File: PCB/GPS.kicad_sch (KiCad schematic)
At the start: 20 parts, among them CN2 Solder_Jumper-2_Open, U3 BGA725L6E6327FTSA1, U4 ST1S12GR, U5 B39162B4327P810, U6 TESEO-LIV3R

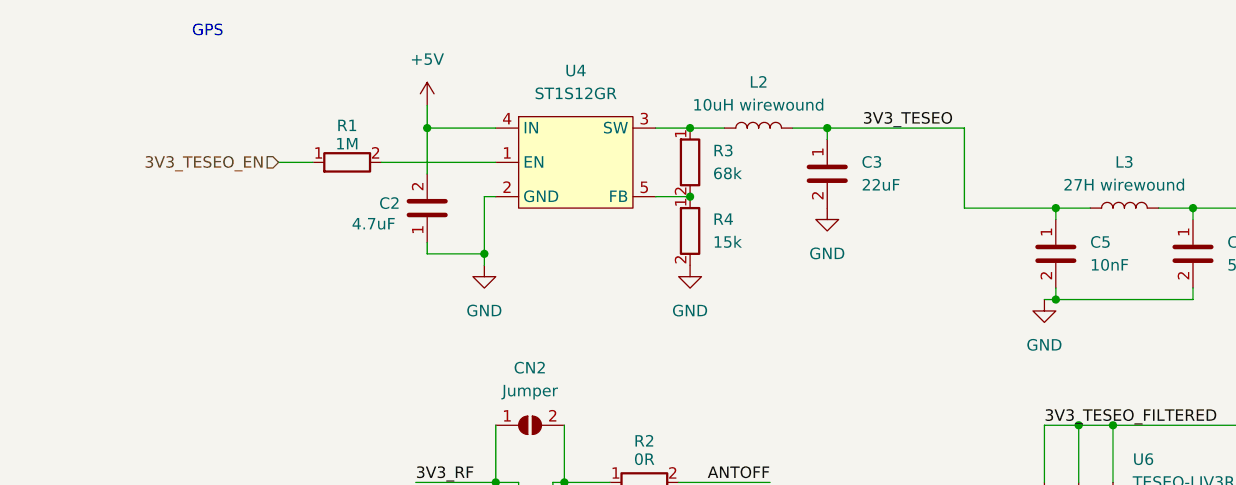
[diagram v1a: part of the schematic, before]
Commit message: Add LEDs
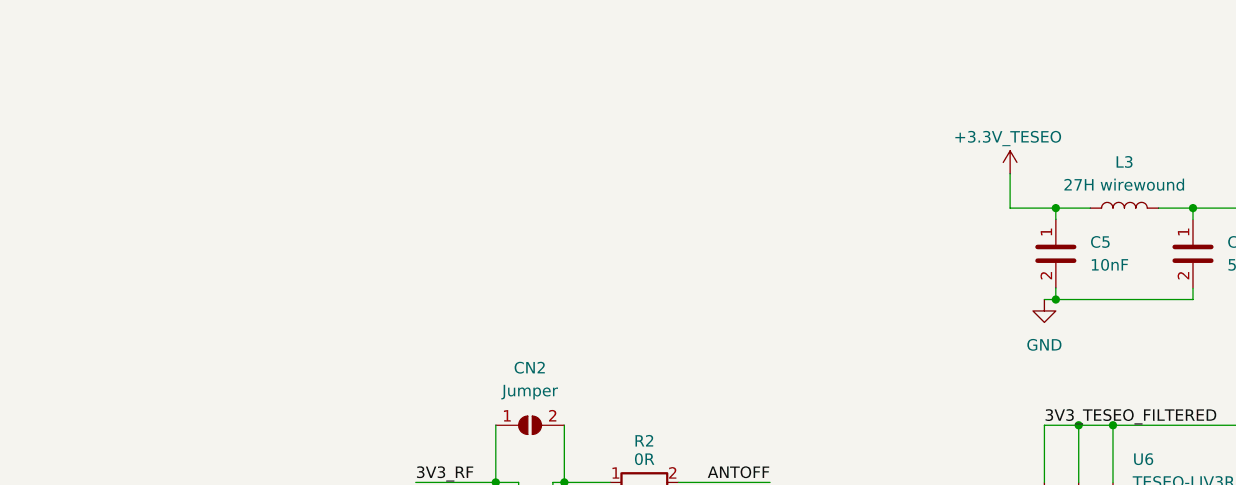
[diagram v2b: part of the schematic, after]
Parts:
- removed C2: C_4.7uF_10V_10%_X7S_0603_H0.95, 002-Capacitors:C_0603_H0.95, symbol 002-Capacitors:C_4.7uF_10V_10%_X7S_0603
- removed C3: C_22uF_6.3V_20%_X5R_0805_H1.4, 002-Capacitors:C_0805_H1.4, symbol 002-Capacitors:C_22uF_6.3V_20%_X5R_0805
- removed L2: L_10uH_20%_1.51A_160mOhm, 003-Inductors:LTF5022T-100M1R3-D, symbol 003-Inductors:L_10uH_20%_1.51A_160mOhm
- removed R1: R_1M_5%_1/16W_0402, 001-Resistors:R_0402_H0.4, symbol 001-Resistors:R_1M_5%_1/16W_0402
- removed R3: R_68k_1%_1/16W_0402, 001-Resistors:R_0402_H0.4, symbol 001-Resistors:R_68k_1%_1/16W_0402
- removed R4: R_15k_1%_1/16W_0402, 001-Resistors:R_0402_H0.4, symbol 001-Resistors:R_15k_1%_1/16W_0402
- removed U4: ST1S12GR, 004-Power:ST1S12GR, symbol 004-Power:ST1S12GR
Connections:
- net 3V3_TESEO renamed +3.3V_TESEO
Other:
- note removed: "GPS"

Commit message: Finish schematic minus mcu
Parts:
- added TP6, TP7, TP8: TP_square_1mm, 011-Misc:Testpoint_square_1mm, symbol 011-Misc:Testpoint_square_1mm
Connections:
- net TESEO_NRST: now also TP8.
- net TESEO_RX: now also TP7.
- net TESEO_TX: now also TP6.
- net +3.3V_TESEO renamed +3.3V
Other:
- note added: "GPS with passive antenna and LNA"

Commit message: Layout start
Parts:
- removed TP6, TP7, TP8: TP_square_1mm, 011-Misc:Testpoint_square_1mm, symbol 011-Misc:Testpoint_square_1mm
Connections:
- net +3.3V renamed +3.3V_GPS

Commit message: First layout draft
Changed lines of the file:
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@@
+	)
+	(junction
+		(at 198.12 71.12)
+		(diameter 0)
+		(color 0 0 0 0)
 	)
 	(junction
@@
 	(wire
 		(pts
+			(xy 198.12 71.12) (xy 198.12 83.82)
+		)
+		(stroke
+			(width 0)
+			(type default)
+		)
+	)
+	(wire
+		(pts
 			(xy 124.46 102.87) (xy 127 102.87)
 		)
@@
 	(wire
 		(pts
-			(xy 198.12 59.69) (xy 198.12 83.82)
+			(xy 198.12 59.69) (xy 198.12 71.12)
 		)
 		(stroke
@@
 					(unit 1)
 				)
+			)
+		)
+	)
+	(symbol
+		(lib_id "power:PWR_FLAG")
+		(at 198.12 71.12 270)
+		(unit 1)
+		(exclude_from_sim no)
+		(in_bom yes)
+		(on_board yes)
+		(dnp no)
+		(property "Reference" "#FLG05"
+			(at 200.025 71.12 0)
+			(effects
+				(font
+					(size 1.27 1.27)
+				)
+				(hide yes)
+			)
+		)
+		(property "Value" "PWR_FLAG"
+			(at 201.93 71.1199 90)
+			(effects
+				(font
+					(size 1.27 1.27)
+				)
+				(justify left)
+			)
+		)
+		(property "Footprint" ""
+			(at 198.12 71.12 0)
+			(effects
+				(font
+					(size 1.27 1.27)
+				)
+				(hide yes)
+			)
+		)
+		(property "Datasheet" "~"
+			(at 198.12 71.12 0)
+			(effects
+				(font
+					(size 1.27 1.27)
+				)
+				(hide yes)
+			)
+		)
+		(property "Description" "Special symbol for telling ERC where power comes from"
+			(at 198.12 71.12 0)
+			(effects
+				(font
+					(size 1.27 1.27)
+				)
+				(hide yes)
+			)
+		)
+		(pin "1"
+		)
+		(instances
+			(project "relativeGPS"
+				(path "/9255e348-2f0c-48d3-8a71-46491dcb1a12/273de9fc-47df-4bf4-82b9-7faf6b333760"
+					(reference "#FLG05")
+					(unit 1)
+				)

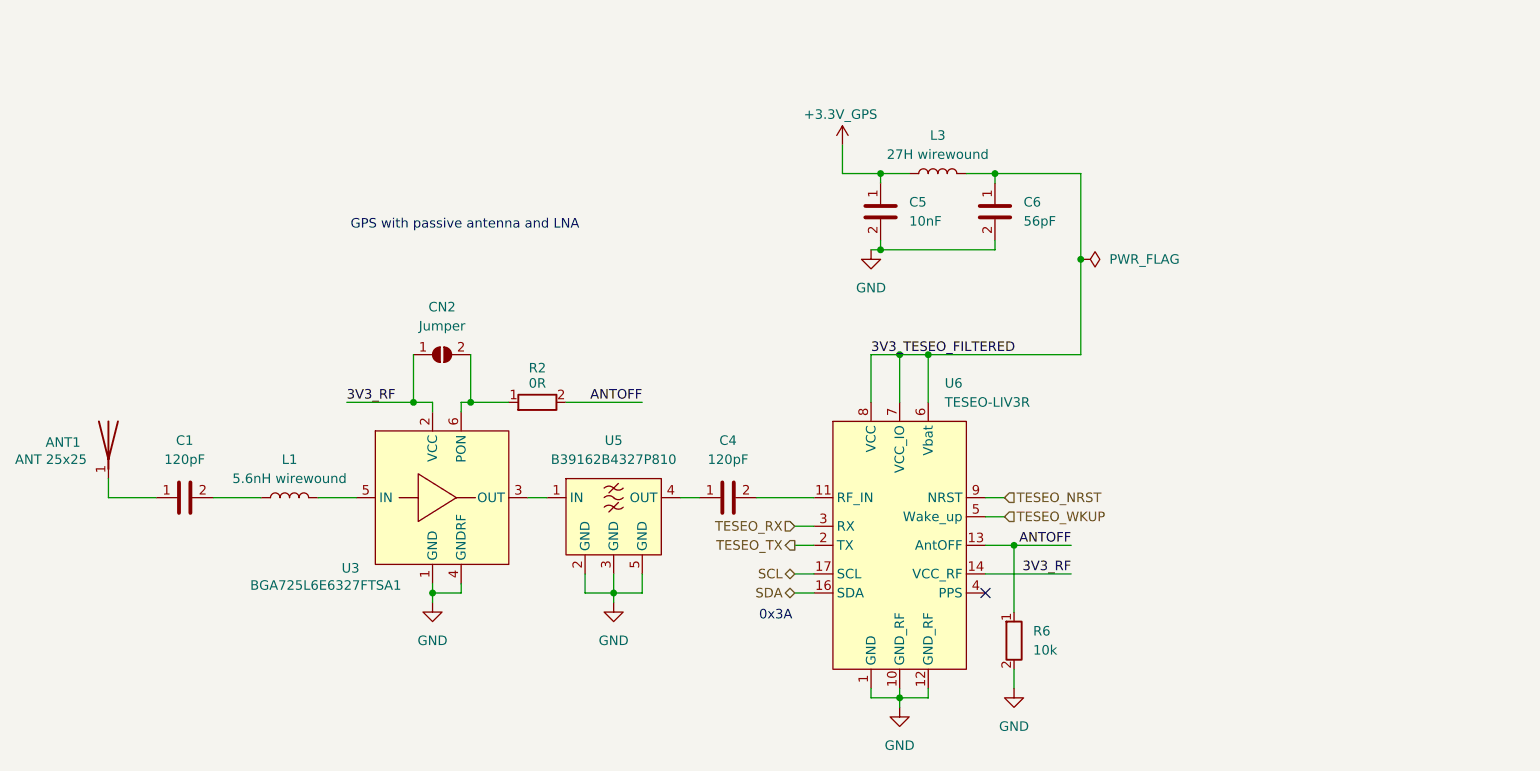
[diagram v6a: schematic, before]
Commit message: Add TPs
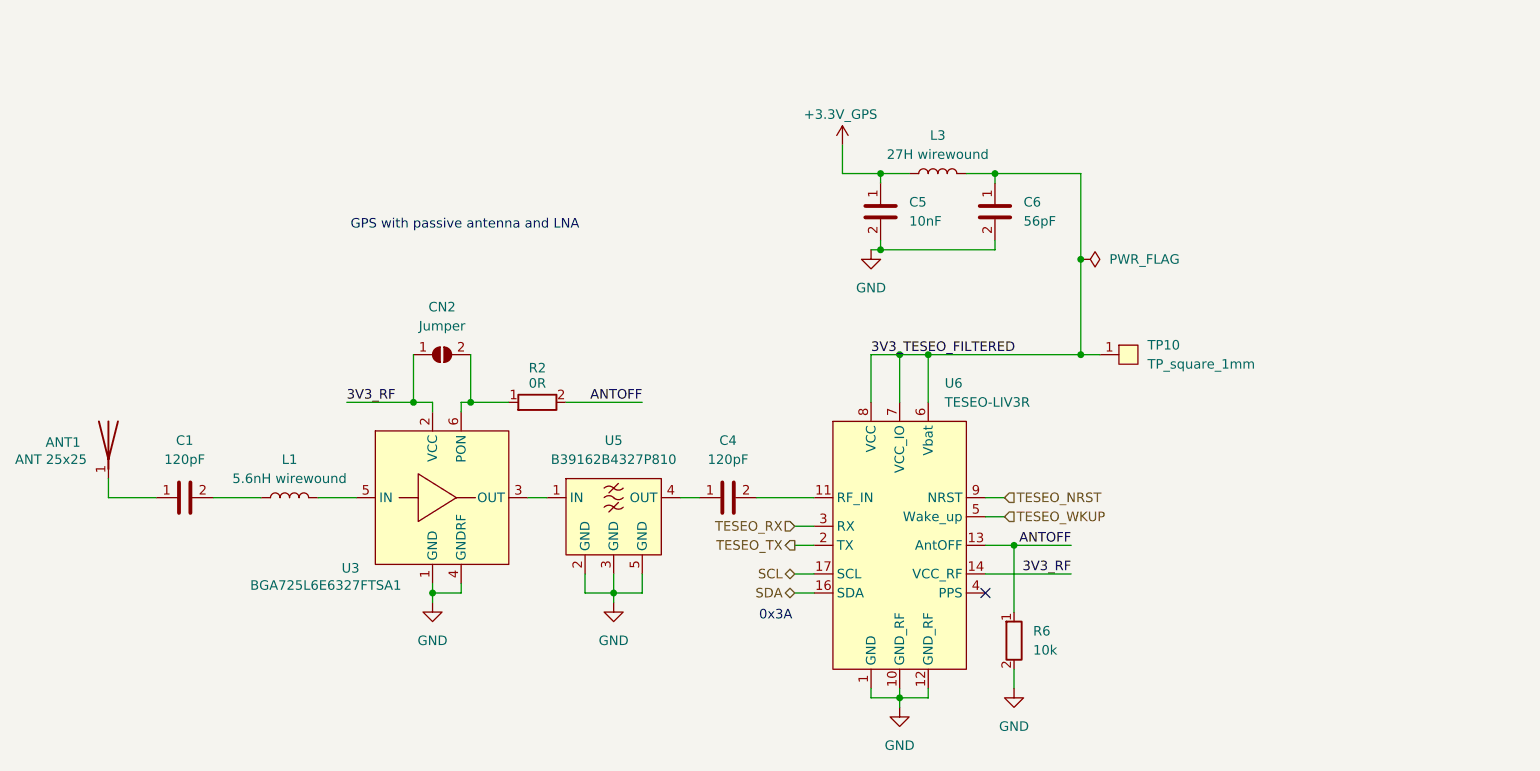
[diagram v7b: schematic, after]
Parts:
- added TP10: TP_square_1mm, 011-Misc:Testpoint_square_1mm, symbol 011-Misc:Testpoint_square_1mm
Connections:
- net 3V3_TESEO_FILTERED: now also TP10.1
